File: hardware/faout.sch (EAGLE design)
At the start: 83 parts, among them IC2 MT48LC64M4A2, Q1 12MHz, Q2 ASFL, U1 LTC3419EMS, U2 93C46B, U3 FLASH-SPI-25XXSMD1, U4 6SLX9TQG144

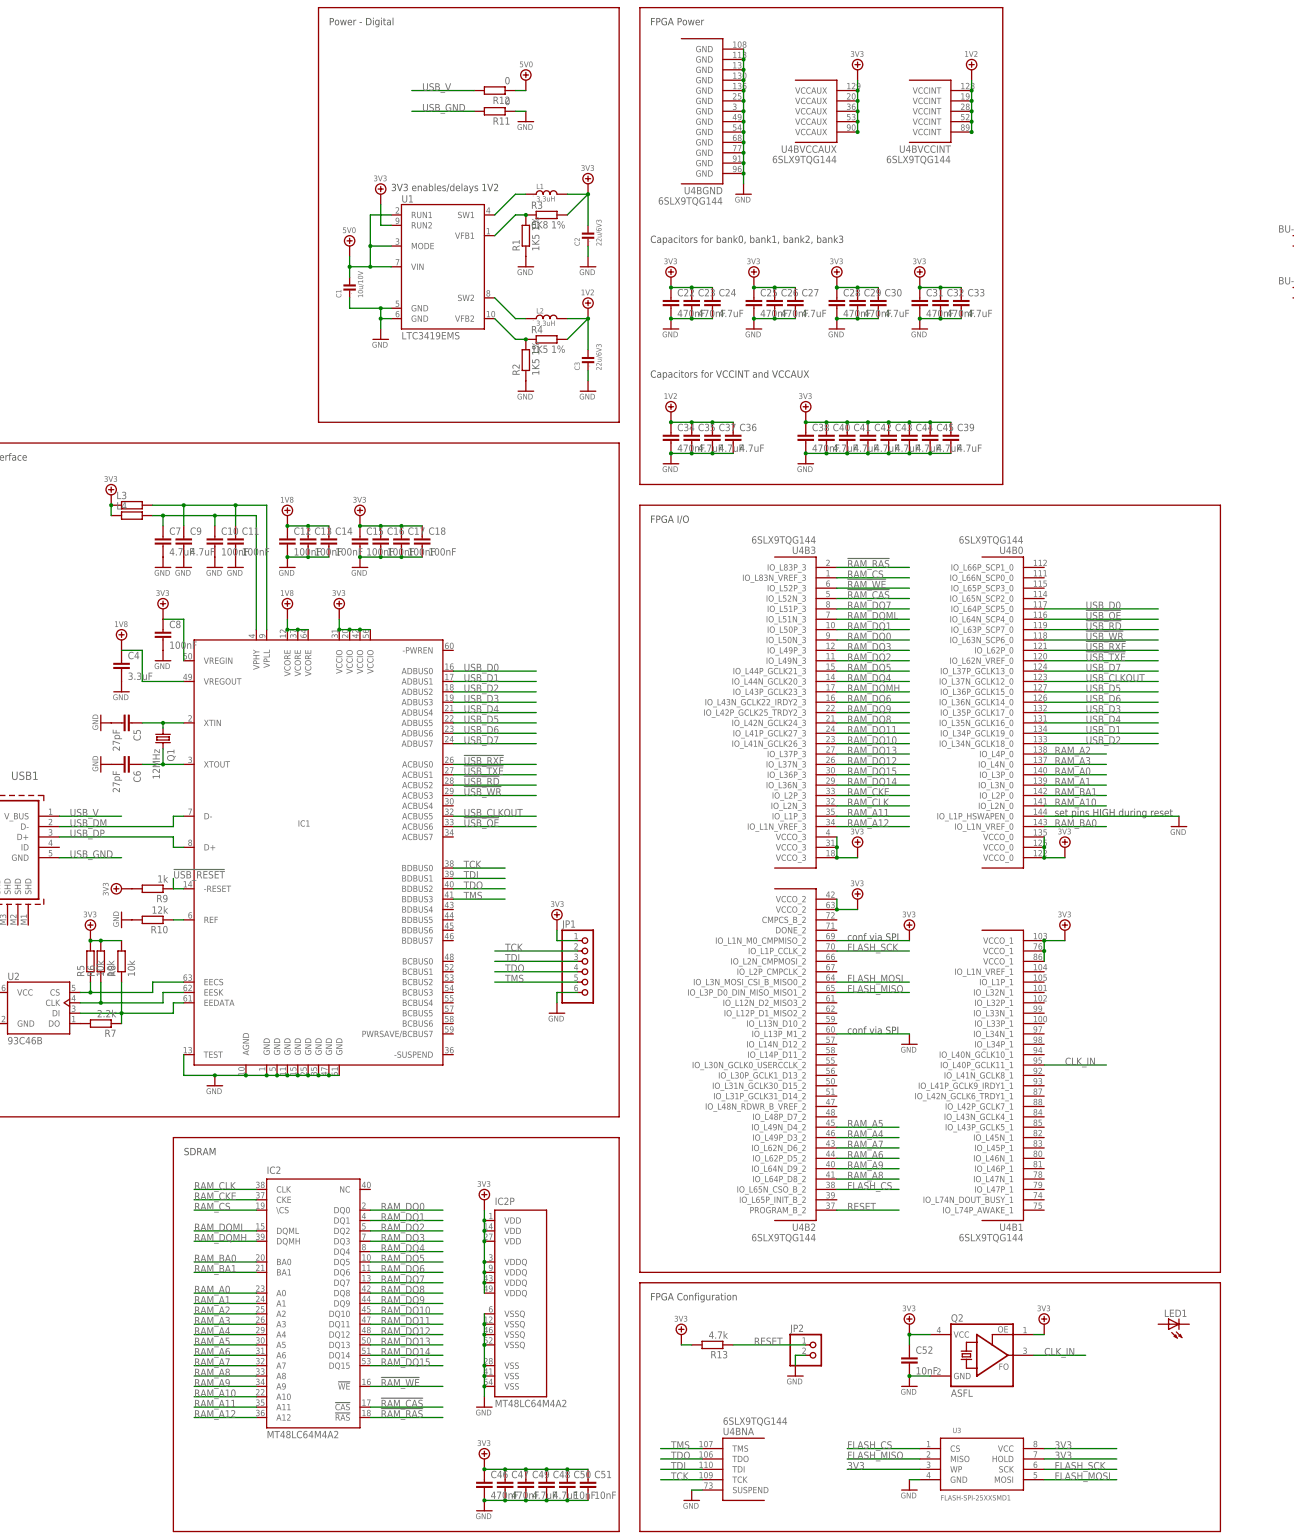
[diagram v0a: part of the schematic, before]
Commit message: Development of FAout hardware.
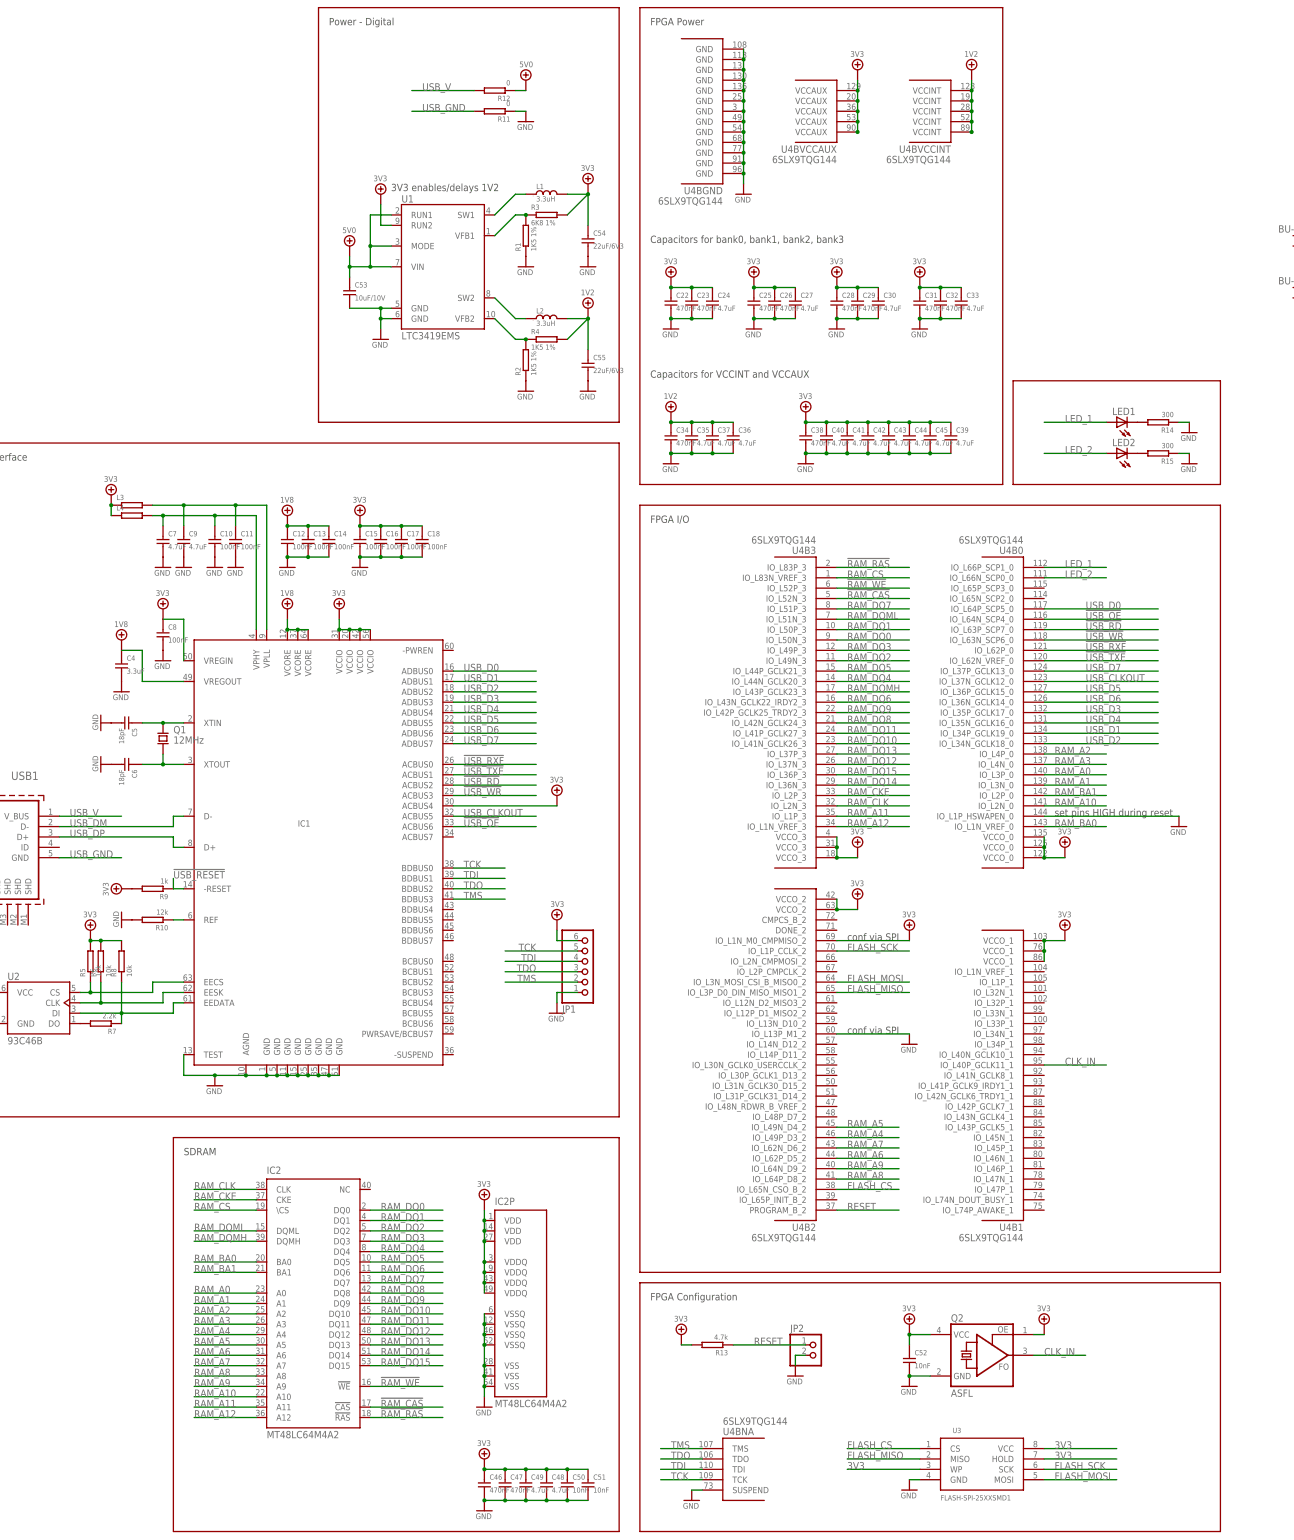
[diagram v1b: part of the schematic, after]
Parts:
- removed C1: 10u/10V, Bogdan_Commons:C0805
- removed C2, C3: 22u/6V3, Bogdan_Commons:C0805
- added C53: 10uF/10V, faout:C_EU0805
- added C54, C55: 22uF/6V3, faout:C_EU0805
- added LED2: (no value), led:LEDSML0805
- added R14, R15: 300, faout:R_EU0603
- C10, C11, C12, C13, C14, C15, C16, C17, C18, C22, C23, C24, C25, C26, C27, C28, C29, C30, C31, C32, C33, C34, C35, C36, C37, C38, C39, C4, C40, C41, C42, C43, C44, C45, C46, C47, C48, C49, C50, C51, C52, C7, C8, C9: device rcl:C-EUC0603K -> faout:C_EU0603
- C5, C6: value 27pF -> 18pF; device rcl:C-EUC0603K -> faout:C_EU0603
- L3, L4, R1, R10, R11, R12, R13, R2, R3, R4, R5, R6, R7, R8, R9: device rcl:R-EU_R0603 -> faout:R_EU0603
- Q1: device crystal:CRYSTALCTS406 -> faout:TXC_QUARTZ_7A; OC_FARNELL 1611798 -> 1841940
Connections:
- new net LED_1: LED1.A, U4B0.IO_L66P_SCP1_0
- new net LED_2: LED2.A, U4B0.IO_L66N_SCP0_0
- new net N$3: LED1.C, R14.P$2
- new net N$4: LED2.C, R15.P$2
- net !USB_RESET: now also R9.P$1; no longer R9.1
- net 1V2: now also C34.P$1, C35.P$1, C36.P$1, C37.P$1, C55.P$1, R4.P$2; no longer C3.2, C34.1, C35.1, C36.1, C37.1, R4.2
- net 1V8: now also C12.P$1, C13.P$1, C14.P$1, C4.P$1; no longer C12.1, C13.1, C14.1, C4.1
- net 3V3: now also C15.P$1, C16.P$1, C17.P$1, C18.P$1, C22.P$1, C23.P$1, C24.P$1, C25.P$1, C26.P$1, C27.P$1, C28.P$1, C29.P$1, C30.P$1, C31.P$1, C32.P$1, C33.P$1, C38.P$1, C39.P$1, C40.P$1, C41.P$1, C42.P$1, C43.P$1, C44.P$1, C45.P$1, C46.P$1, C47.P$1, C48.P$1, C49.P$1, C50.P$1, C51.P$1, C52.P$1, C54.P$1, C8.P$1, IC1.ACBUS4, JP1.6, L3.P$1, L4.P$1, R13.P$2, R3.P$2, R5.P$2, R6.P$2, R8.P$2, R9.P$2; no longer C15.1, C16.1, C17.1, C18.1, C2.2, C22.1, C23.1, C24.1, C25.1, C26.1, C27.1, C28.1, C29.1, C30.1, C31.1, C32.1, C33.1, C38.1, C39.1, C40.1, C41.1, C42.1, C43.1, C44.1, C45.1, C46.1, C47.1, C48.1, C49.1, C50.1, C51.1, C52.1, C8.1, JP1.1, L3.1, L4.1, R13.2, R3.2, R5.2, R6.2, R8.2, R9.2
- net 5V0: now also C53.P$1, R12.P$1; no longer C1.2, R12.1
- net EECS: now also R5.P$1; no longer R5.1
- net EEDATA: now also R7.P$1, R8.P$1; no longer R7.1, R8.1
- net EESK: now also R6.P$1; no longer R6.1
- net FB_1V2: now also R2.P$2, R4.P$1; no longer R2.2, R4.1
- net FB_3V3: now also R1.P$2, R3.P$1; no longer R1.2, R3.1
- net GND: now also C10.P$2, C11.P$2, C12.P$2, C13.P$2, C14.P$2, C15.P$2, C16.P$2, C17.P$2, C18.P$2, C22.P$2, C23.P$2, C24.P$2, C25.P$2, C26.P$2, C27.P$2, C28.P$2, C29.P$2, C30.P$2, C31.P$2, C32.P$2, C33.P$2, C34.P$2, C35.P$2, C36.P$2, C37.P$2, C38.P$2, C39.P$2, C4.P$2, C40.P$2, C41.P$2, C42.P$2, C43.P$2, C44.P$2, C45.P$2, C46.P$2, C47.P$2, C48.P$2, C49.P$2, C5.P$2, C50.P$2, C51.P$2, C52.P$2, C53.P$2, C54.P$2, C55.P$2, C6.P$2, C7.P$2, C8.P$2, C9.P$2, JP1.1, R1.P$1, R10.P$2, R11.P$1, R14.P$1, R15.P$1, R2.P$1; no longer C1.1, C10.2, C11.2, C12.2, C13.2, C14.2, C15.2, C16.2, C17.2, C18.2, C2.1, C22.2, C23.2, C24.2, C25.2, C26.2, C27.2, C28.2, C29.2, C3.1, C30.2, C31.2, C32.2, C33.2, C34.2, C35.2, C36.2, C37.2, C38.2, C39.2, C4.2, C40.2, C41.2, C42.2, C43.2, C44.2, C45.2, C46.2, C47.2, C48.2, C49.2, C5.2, C50.2, C51.2, C52.2, C6.2, C7.2, C8.2, C9.2, JP1.6, R1.1, R10.2, R11.1, R2.1
- net N$1: now also C5.P$1, Q1.P$1; no longer C5.1, Q1.1
- net N$2: now also C6.P$1, Q1.P$2; no longer C6.1, Q1.2
- net N$5: now also C10.P$1, C7.P$1, L4.P$2; no longer C10.1, C7.1, L4.2
- net N$6: now also R7.P$2; no longer R7.2
- net N$7: now also C11.P$1, C9.P$1, L3.P$2; no longer C11.1, C9.1, L3.2
- net RESET: now also R13.P$1; no longer R13.1
- net USB_GND: now also R11.P$2; no longer R11.2
- net USB_REF: now also R10.P$1; no longer R10.1
- net USB_V: now also R12.P$2; no longer R12.2
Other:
- moved on the sheet: JP1, LED1, Q1

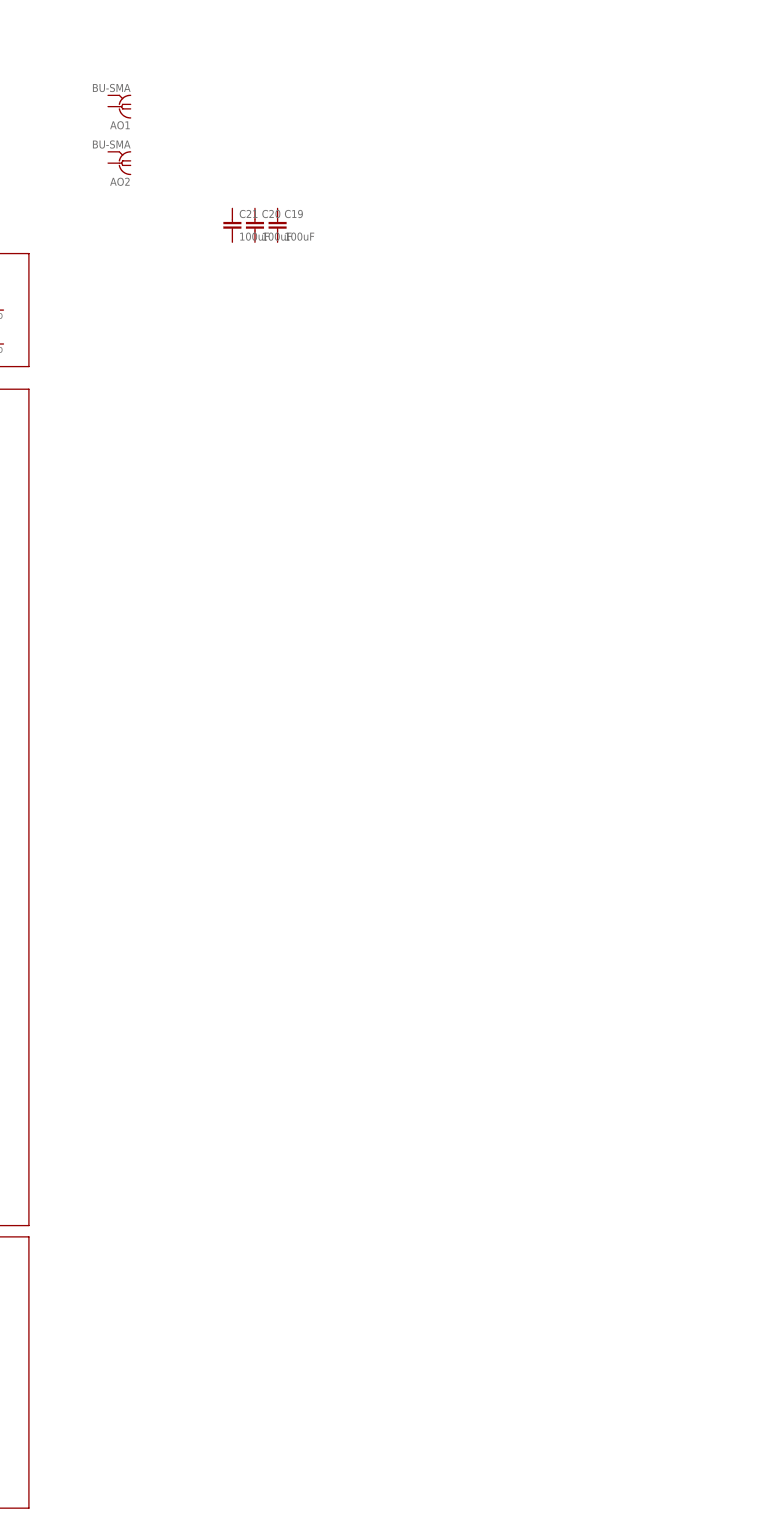
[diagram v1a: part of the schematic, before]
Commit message: Add DAC converters.
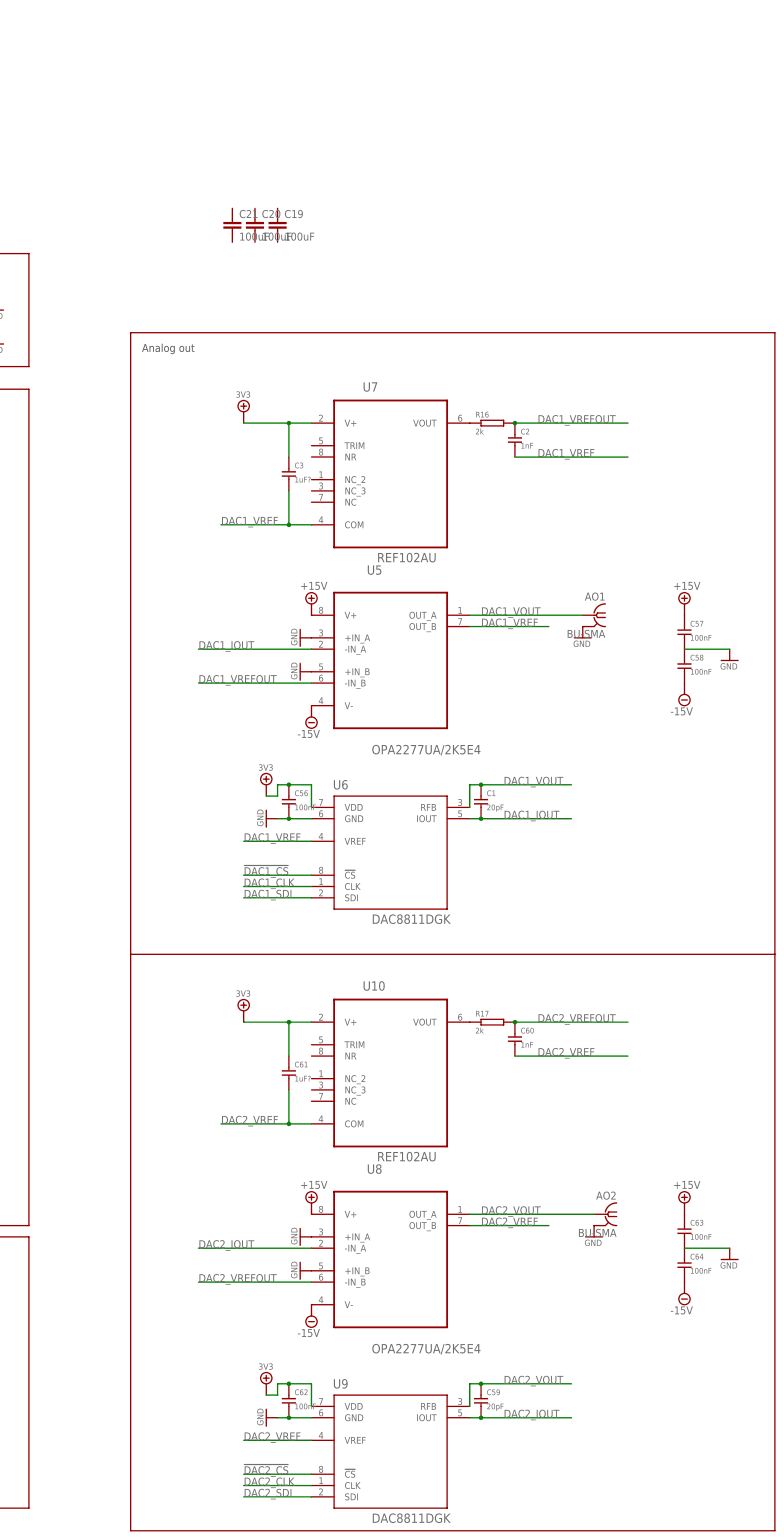
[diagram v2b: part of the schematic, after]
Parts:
- added C1, C59: 20pF, faout:C_EU0603
- added C2, C60: 1nF, faout:C_EU0603
- added C3, C61: 1uF?, faout:C_EU0603
- added C56, C57, C58, C62, C63, C64: 100nF, faout:C_EU0603
- added R16, R17: 2k, faout:R_EU0603
- added U10, U7: REF102AU, faout:REF102AU
- added U5, U8: OPA2277UA/2K5E4, faout:OPA2277UA/2K5E4
- added U6, U9: DAC8811DGK, faout:DAC8811DGK
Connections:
- new net !DAC1_CS: U6.!CS
- new net !DAC2_CS: U9.!CS
- new net +15V: C57.P$1, C63.P$1, U5.V+, U8.V+
- new net -15V: C58.P$2, C64.P$2, U5.V-, U8.V-
- new net DAC1_CLK: U6.CLK
- new net DAC1_IOUT: C1.P$2, U5.-IN_A, U6.IOUT
- new net DAC1_SDI: U6.SDI
- new net DAC1_VOUT: AO1.1, C1.P$1, U5.OUT_A, U6.RFB
- new net DAC1_VREF: C2.P$2, C3.P$2, U5.OUT_B, U6.VREF, U7.COM
- new net DAC1_VREFOUT: C2.P$1, R16.P$2, U5.-IN_B
- new net DAC2_CLK: U9.CLK
- new net DAC2_IOUT: C59.P$2, U8.-IN_A, U9.IOUT
- new net DAC2_SDI: U9.SDI
- new net DAC2_VOUT: AO2.1, C59.P$1, U8.OUT_A, U9.RFB
- new net DAC2_VREF: C60.P$2, C61.P$2, U10.COM, U8.OUT_B, U9.VREF
- new net DAC2_VREFOUT: C60.P$1, R17.P$2, U8.-IN_B
- new net N$10: R16.P$1, U7.VOUT
- new net N$8: R17.P$1, U10.VOUT
- net 3V3: now also C3.P$1, C56.P$1, C61.P$1, C62.P$1, U10.V+, U6.VDD, U7.V+, U9.VDD
- net GND: now also AO1.2, AO2.2, C56.P$2, C57.P$2, C58.P$1, C62.P$2, C63.P$2, C64.P$1, U5.+IN_A, U5.+IN_B, U6.GND, U8.+IN_A, U8.+IN_B, U9.GND
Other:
- note added: "Analog out"
- moved on the sheet: AO1, AO2
